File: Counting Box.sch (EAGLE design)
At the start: 3 parts

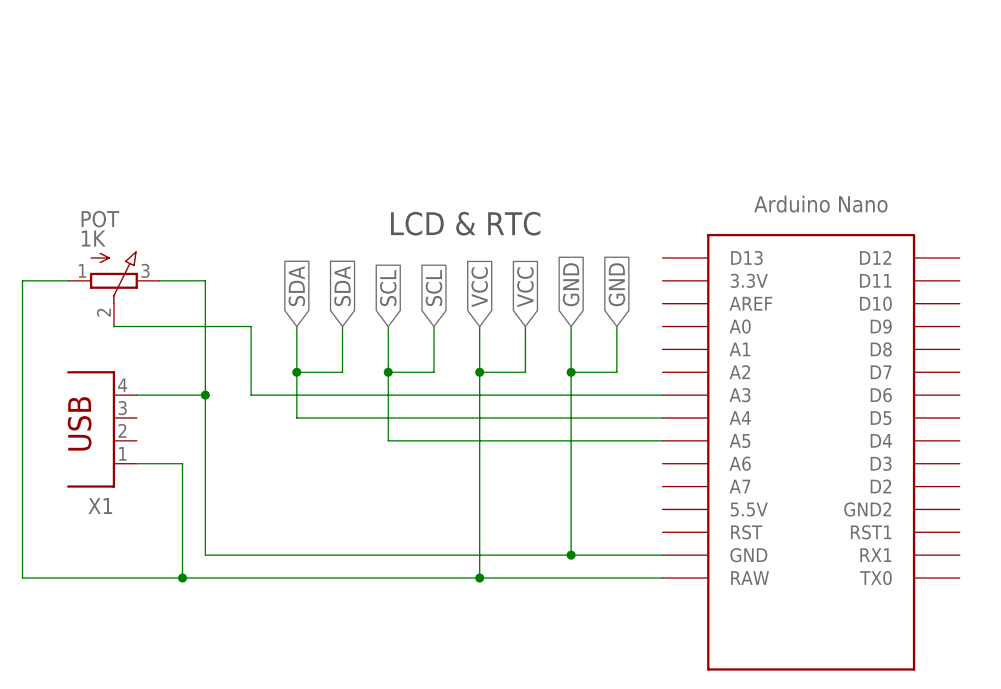
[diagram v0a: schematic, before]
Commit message: Eagle board, code fixes.
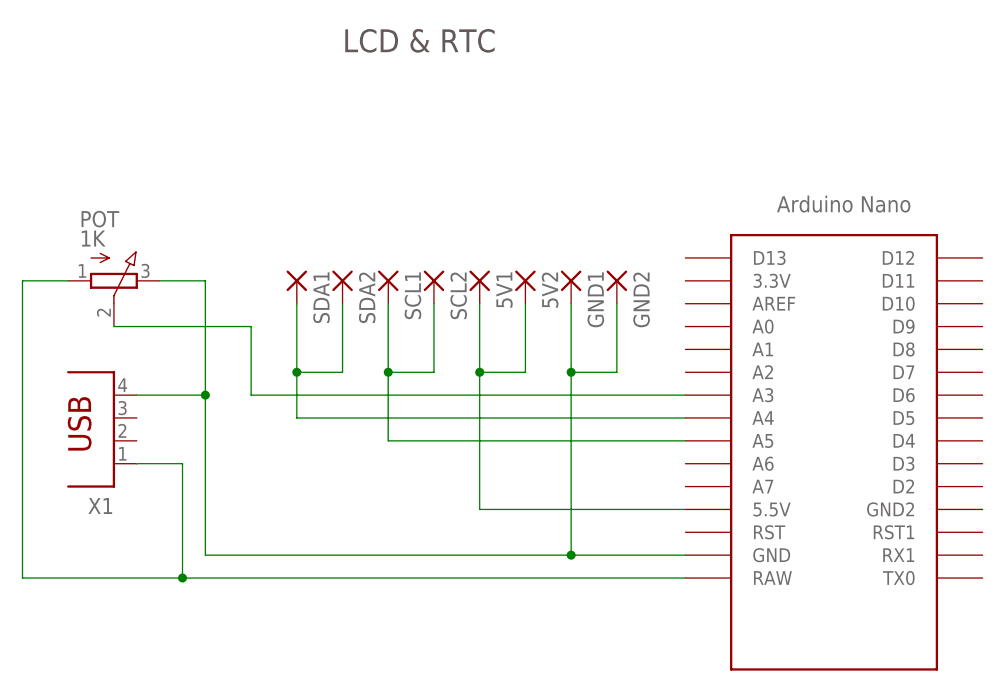
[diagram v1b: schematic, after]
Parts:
- added 5V1, 5V2, GND1, GND2, SCL1, SCL2, SDA1, SDA2: (no value), wirepad:SMD2
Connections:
- net N$3 renamed POT_CTRL
- new net 5V: 5V1.P, 5V2.P, U$1.5.5V
- net GND: now also GND1.P, GND2.P
- net SCL: now also SCL1.P, SCL2.P
- net SDA: now also SDA1.P, SDA2.P
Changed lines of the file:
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@@
 <part name="POT" library="pot" library_urn="urn:adsk.eagle:library:331" deviceset="3RP/1610N" device="" package3d_urn="urn:adsk.eagle:package:22726/1" value="1K"/>
 <part name="X1" library="con-berg" library_urn="urn:adsk.eagle:library:130" deviceset="PN87520" device="" package3d_urn="urn:adsk.eagle:package:6146/1"/>
+<part name="SDA1" library="wirepad" library_urn="urn:adsk.eagle:library:412" deviceset="SMD2" device="" package3d_urn="urn:adsk.eagle:package:30839/1"/>
+<part name="SDA2" library="wirepad" library_urn="urn:adsk.eagle:library:412" deviceset="SMD2" device="" package3d_urn="urn:adsk.eagle:package:30839/1"/>
+<part name="SCL1" library="wirepad" library_urn="urn:adsk.eagle:library:412" deviceset="SMD2" device="" package3d_urn="urn:adsk.eagle:package:30839/1"/>
+<part name="SCL2" library="wirepad" library_urn="urn:adsk.eagle:library:412" deviceset="SMD2" device="" package3d_urn="urn:adsk.eagle:package:30839/1"/>
+<part name="5V1" library="wirepad" library_urn="urn:adsk.eagle:library:412" deviceset="SMD2" device="" package3d_urn="urn:adsk.eagle:package:30839/1"/>
+<part name="5V2" library="wirepad" library_urn="urn:adsk.eagle:library:412" deviceset="SMD2" device="" package3d_urn="urn:adsk.eagle:package:30839/1"/>
+<part name="GND1" library="wirepad" library_urn="urn:adsk.eagle:library:412" deviceset="SMD2" device="" package3d_urn="urn:adsk.eagle:package:30839/1"/>
+<part name="GND2" library="wirepad" library_urn="urn:adsk.eagle:library:412" deviceset="SMD2" device="" package3d_urn="urn:adsk.eagle:package:30839/1"/>
 </parts>
 <sheets>
 <sheet>
 <plain>
-<text x="22.86" y="66.04" size="2.54" layer="97">LCD &amp; RTC</text>
+<text x="17.78" y="86.36" size="2.54" layer="97">LCD &amp; RTC</text>
 </plain>
 <instances>
-<instance part="U$1" gate="G$1" x="76.2" y="48.26"/>
+<instance part="U$1" gate="G$1" x="78.74" y="48.26"/>
 <instance part="POT" gate="G$1" x="-7.62" y="60.96" rot="R270"/>
 <instance part="X1" gate="G$1" x="-7.62" y="45.72" rot="R180"/>
+<instance part="SDA1" gate="1" x="12.7" y="60.96" rot="R270"/>
+<instance part="SDA2" gate="1" x="17.78" y="60.96" rot="R270"/>
+<instance part="SCL1" gate="1" x="22.86" y="60.96" rot="R270"/>
+<instance part="SCL2" gate="1" x="27.94" y="60.96" rot="R270"/>
+<instance part="5V1" gate="1" x="33.02" y="60.96" rot="R270"/>
+<instance part="5V2" gate="1" x="38.1" y="60.96" rot="R270"/>
+<instance part="GND1" gate="1" x="43.18" y="60.96" rot="R270"/>
+<instance part="GND2" gate="1" x="48.26" y="60.96" rot="R270"/>
 </instances>
 <busses>
@@
 <wire x1="0" y1="40.64" x2="0" y2="27.94" width="0.1524" layer="91"/>
 <pinref part="U$1" gate="G$1" pin="RAW"/>
-<wire x1="0" y1="27.94" x2="33.02" y2="27.94" width="0.1524" layer="91"/>
-<wire x1="33.02" y1="27.94" x2="53.34" y2="27.94" width="0.1524" layer="91"/>
+<wire x1="0" y1="27.94" x2="55.88" y2="27.94" width="0.1524" layer="91"/>
 <wire x1="0" y1="27.94" x2="-17.78" y2="27.94" width="0.1524" layer="91"/>
 <junction x="0" y="27.94"/>
@@
 <wire x1="-17.78" y1="27.94" x2="-17.78" y2="60.96" width="0.1524" layer="91"/>
 <wire x1="-17.78" y1="60.96" x2="-12.7" y2="60.96" width="0.1524" layer="91"/>
-<wire x1="33.02" y1="50.8" x2="33.02" y2="27.94" width="0.1524" layer="91"/>
-<junction x="33.02" y="27.94"/>
-<wire x1="33.02" y1="50.8" x2="38.1" y2="50.8" width="0.1524" layer="91"/>
-<wire x1="38.1" y1="50.8" x2="38.1" y2="55.88" width="0.1524" layer="91"/>
-<wire x1="33.02" y1="50.8" x2="33.02" y2="55.88" width="0.1524" layer="91"/>
-<junction x="33.02" y="50.8"/>
-<label x="33.02" y="55.88" size="1.778" layer="95" rot="R90" xref="yes"/>
-<label x="38.1" y="55.88" size="1.778" layer="95" rot="R90" xref="yes"/>
 </segment>
 </net>
@@
 <pinref part="U$1" gate="G$1" pin="GND"/>
 <wire x1="2.54" y1="30.48" x2="43.18" y2="30.48" width="0.1524" layer="91"/>
-<wire x1="43.18" y1="30.48" x2="53.34" y2="30.48" width="0.1524" layer="91"/>
+<wire x1="43.18" y1="30.48" x2="55.88" y2="30.48" width="0.1524" layer="91"/>
 <wire x1="2.54" y1="30.48" x2="2.54" y2="48.26" width="0.1524" layer="91"/>
 <pinref part="POT" gate="G$1" pin="E"/>
@@
 <wire x1="-5.08" y1="48.26" x2="2.54" y2="48.26" width="0.1524" layer="91"/>
 <junction x="2.54" y="48.26"/>
-<wire x1="43.18" y1="55.88" x2="43.18" y2="50.8" width="0.1524" layer="91"/>
+<wire x1="43.18" y1="58.42" x2="43.18" y2="50.8" width="0.1524" layer="91"/>
 <junction x="43.18" y="30.48"/>
 <wire x1="43.18" y1="50.8" x2="43.18" y2="30.48" width="0.1524" layer="91"/>
 <wire x1="43.18" y1="50.8" x2="48.26" y2="50.8" width="0.1524" layer="91"/>
 <junction x="43.18" y="50.8"/>
-<wire x1="48.26" y1="50.8" x2="48.26" y2="55.88" width="0.1524" layer="91"/>
-<label x="43.18" y="55.88" size="1.778" layer="95" rot="R90" xref="yes"/>
-<label x="48.26" y="55.88" size="1.778" layer="95" rot="R90" xref="yes"/>
+<wire x1="48.26" y1="50.8" x2="48.26" y2="58.42" width="0.1524" layer="91"/>
+<pinref part="GND1" gate="1" pin="P"/>
+<pinref part="GND2" gate="1" pin="P"/>
 </segment>
 </net>
-<net name="N$3" class="0">
+<net name="POT_CTRL" class="0">
 <segment>
 <pinref part="U$1" gate="G$1" pin="A3"/>
-<wire x1="53.34" y1="48.26" x2="7.62" y2="48.26" width="0.1524" layer="91"/>
+<wire x1="55.88" y1="48.26" x2="7.62" y2="48.26" width="0.1524" layer="91"/>
 <wire x1="7.62" y1="48.26" x2="7.62" y2="55.88" width="0.1524" layer="91"/>
 <wire x1="7.62" y1="55.88" x2="-7.62" y2="55.88" width="0.1524" layer="91"/>
@@
 <segment>
 <pinref part="U$1" gate="G$1" pin="A4"/>
-<wire x1="53.34" y1="45.72" x2="12.7" y2="45.72" width="0.1524" layer="91"/>
+<wire x1="55.88" y1="45.72" x2="12.7" y2="45.72" width="0.1524" layer="91"/>
 <wire x1="12.7" y1="45.72" x2="12.7" y2="50.8" width="0.1524" layer="91"/>
 <wire x1="12.7" y1="50.8" x2="17.78" y2="50.8" width="0.1524" layer="91"/>
-<wire x1="17.78" y1="50.8" x2="17.78" y2="55.88" width="0.1524" layer="91"/>
-<wire x1="12.7" y1="50.8" x2="12.7" y2="55.88" width="0.1524" layer="91"/>
+<wire x1="17.78" y1="50.8" x2="17.78" y2="58.42" width="0.1524" layer="91"/>
+<wire x1="12.7" y1="50.8" x2="12.7" y2="58.42" width="0.1524" layer="91"/>
 <junction x="12.7" y="50.8"/>
-<label x="12.7" y="55.88" size="1.778" layer="95" rot="R90" xref="yes"/>
-<label x="17.78" y="55.88" size="1.778" layer="95" rot="R90" xref="yes"/>
+<pinref part="SDA1" gate="1" pin="P"/>
+<pinref part="SDA2" gate="1" pin="P"/>
 </segment>
 </net>
@@
 <segment>
 <pinref part="U$1" gate="G$1" pin="A5"/>
-<wire x1="53.34" y1="43.18" x2="22.86" y2="43.18" width="0.1524" layer="91"/>
+<wire x1="55.88" y1="43.18" x2="22.86" y2="43.18" width="0.1524" layer="91"/>
 <wire x1="22.86" y1="43.18" x2="22.86" y2="50.8" width="0.1524" layer="91"/>
 <wire x1="22.86" y1="50.8" x2="27.94" y2="50.8" width="0.1524" layer="91"/>
-<wire x1="27.94" y1="50.8" x2="27.94" y2="55.88" width="0.1524" layer="91"/>
-<wire x1="22.86" y1="50.8" x2="22.86" y2="55.88" width="0.1524" layer="91"/>
+<wire x1="27.94" y1="50.8" x2="27.94" y2="58.42" width="0.1524" layer="91"/>
+<wire x1="22.86" y1="50.8" x2="22.86" y2="58.42" width="0.1524" layer="91"/>
 <junction x="22.86" y="50.8"/>
-<label x="22.86" y="55.88" size="1.778" layer="95" rot="R90" xref="yes"/>
-<label x="27.94" y="55.88" size="1.778" layer="95" rot="R90" xref="yes"/>
+<pinref part="SCL1" gate="1" pin="P"/>
+<pinref part="SCL2" gate="1" pin="P"/>
 </segment>
 </net>
+<net name="5V" class="0">
+<segment>
+<wire x1="38.1" y1="50.8" x2="38.1" y2="58.42" width="0.1524" layer="91"/>
+<wire x1="33.02" y1="50.8" x2="38.1" y2="50.8" width="0.1524" layer="91"/>
+<wire x1="33.02" y1="50.8" x2="33.02" y2="58.42" width="0.1524" layer="91"/>
+<junction x="33.02" y="50.8"/>
+<wire x1="33.02" y1="50.8" x2="33.02" y2="35.56" width="0.1524" layer="91"/>
+<pinref part="U$1" gate="G$1" pin="5.5V"/>
+<wire x1="55.88" y1="35.56" x2="33.02" y2="35.56" width="0.1524" layer="91"/>
+<pinref part="5V1" gate="1" pin="P"/>
+<pinref part="5V2" gate="1" pin="P"/>
+</segment>
+</net>

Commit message: Added second potentiometer to schematic.
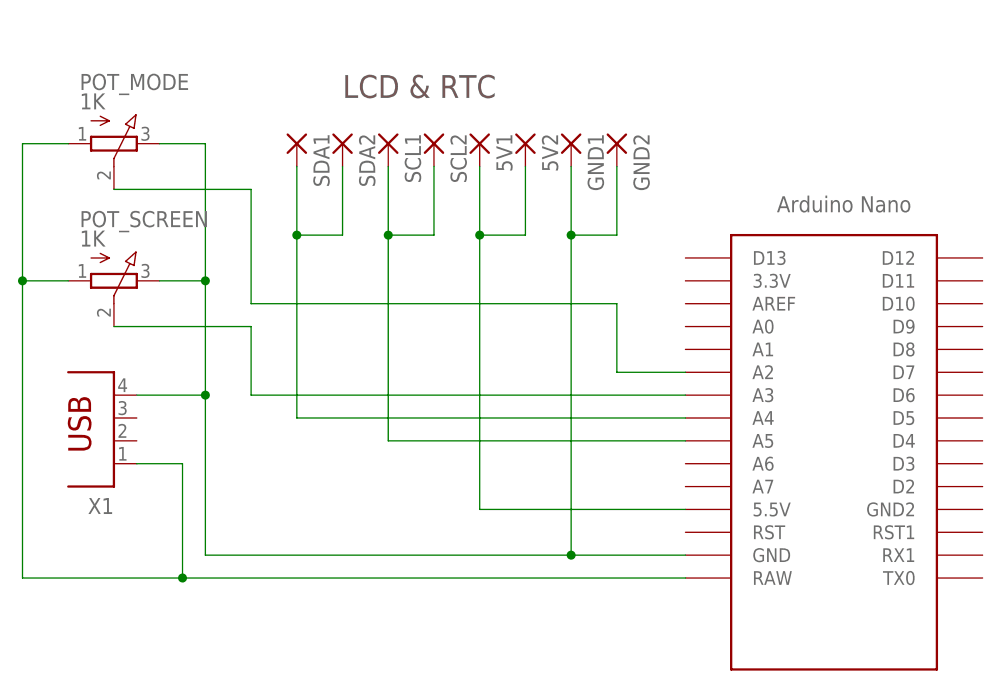
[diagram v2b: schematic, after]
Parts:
- added POT_MODE: 1K, pot:3RP/1610N
- renumbered POT to POT_SCREEN
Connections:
- new net N$5: POT_MODE.S, U$1.A2
- net GND: now also POT_MODE.E
- net VCC: now also POT_MODE.A
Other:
- moved on the sheet: 5V1, 5V2, GND1, GND2, SCL1, SCL2, SDA1, SDA2
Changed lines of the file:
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@@
 <?xml version="1.0" encoding="utf-8"?>
 <!DOCTYPE eagle SYSTEM "eagle.dtd">
-<eagle version="8.4.0">
+<eagle version="8.5.1">
 <drawing>
 <settings>
@@
 <parts>
 <part name="U$1" library="Arduino-clone" deviceset="NANO" device=""/>
-<part name="POT" library="pot" library_urn="urn:adsk.eagle:library:331" deviceset="3RP/1610N" device="" package3d_urn="urn:adsk.eagle:package:22726/1" value="1K"/>
+<part name="POT_SCREEN" library="pot" library_urn="urn:adsk.eagle:library:331" deviceset="3RP/1610N" device="" package3d_urn="urn:adsk.eagle:package:22726/1" value="1K"/>
 <part name="X1" library="con-berg" library_urn="urn:adsk.eagle:library:130" deviceset="PN87520" device="" package3d_urn="urn:adsk.eagle:package:6146/1"/>
 <part name="SDA1" library="wirepad" library_urn="urn:adsk.eagle:library:412" deviceset="SMD2" device="" package3d_urn="urn:adsk.eagle:package:30839/1"/>
@@
 <part name="GND1" library="wirepad" library_urn="urn:adsk.eagle:library:412" deviceset="SMD2" device="" package3d_urn="urn:adsk.eagle:package:30839/1"/>
 <part name="GND2" library="wirepad" library_urn="urn:adsk.eagle:library:412" deviceset="SMD2" device="" package3d_urn="urn:adsk.eagle:package:30839/1"/>
+<part name="POT_MODE" library="pot" library_urn="urn:adsk.eagle:library:331" deviceset="3RP/1610N" device="" package3d_urn="urn:adsk.eagle:package:22726/1" value="1K"/>
 </parts>
 <sheets>
 <sheet>
 <plain>
-<text x="17.78" y="86.36" size="2.54" layer="97">LCD &amp; RTC</text>
+<text x="17.78" y="81.28" size="2.54" layer="97">LCD &amp; RTC</text>
 </plain>
 <instances>
 <instance part="U$1" gate="G$1" x="78.74" y="48.26"/>
-<instance part="POT" gate="G$1" x="-7.62" y="60.96" rot="R270"/>
+<instance part="POT_SCREEN" gate="G$1" x="-7.62" y="60.96" rot="R270"/>
 <instance part="X1" gate="G$1" x="-7.62" y="45.72" rot="R180"/>
-<instance part="SDA1" gate="1" x="12.7" y="60.96" rot="R270"/>
-<instance part="SDA2" gate="1" x="17.78" y="60.96" rot="R270"/>
-<instance part="SCL1" gate="1" x="22.86" y="60.96" rot="R270"/>
-<instance part="SCL2" gate="1" x="27.94" y="60.96" rot="R270"/>
-<instance part="5V1" gate="1" x="33.02" y="60.96" rot="R270"/>
-<instance part="5V2" gate="1" x="38.1" y="60.96" rot="R270"/>
-<instance part="GND1" gate="1" x="43.18" y="60.96" rot="R270"/>
-<instance part="GND2" gate="1" x="48.26" y="60.96" rot="R270"/>
+<instance part="SDA1" gate="1" x="12.7" y="76.2" rot="R270"/>
+<instance part="SDA2" gate="1" x="17.78" y="76.2" rot="R270"/>
+<instance part="SCL1" gate="1" x="22.86" y="76.2" rot="R270"/>
+<instance part="SCL2" gate="1" x="27.94" y="76.2" rot="R270"/>
+<instance part="5V1" gate="1" x="33.02" y="76.2" rot="R270"/>
+<instance part="5V2" gate="1" x="38.1" y="76.2" rot="R270"/>
+<instance part="GND1" gate="1" x="43.18" y="76.2" rot="R270"/>
+<instance part="GND2" gate="1" x="48.26" y="76.2" rot="R270"/>
+<instance part="POT_MODE" gate="G$1" x="-7.62" y="76.2" rot="R270"/>
 </instances>
 <busses>
@@
 <wire x1="0" y1="27.94" x2="-17.78" y2="27.94" width="0.1524" layer="91"/>
 <junction x="0" y="27.94"/>
-<pinref part="POT" gate="G$1" pin="A"/>
+<pinref part="POT_SCREEN" gate="G$1" pin="A"/>
 <wire x1="-17.78" y1="27.94" x2="-17.78" y2="60.96" width="0.1524" layer="91"/>
 <wire x1="-17.78" y1="60.96" x2="-12.7" y2="60.96" width="0.1524" layer="91"/>
+<wire x1="-17.78" y1="60.96" x2="-17.78" y2="76.2" width="0.1524" layer="91"/>
+<junction x="-17.78" y="60.96"/>
+<pinref part="POT_MODE" gate="G$1" pin="A"/>
+<wire x1="-17.78" y1="76.2" x2="-12.7" y2="76.2" width="0.1524" layer="91"/>
 </segment>
 </net>
@@
 <wire x1="43.18" y1="30.48" x2="55.88" y2="30.48" width="0.1524" layer="91"/>
 <wire x1="2.54" y1="30.48" x2="2.54" y2="48.26" width="0.1524" layer="91"/>
-<pinref part="POT" gate="G$1" pin="E"/>
+<pinref part="POT_SCREEN" gate="G$1" pin="E"/>
 <wire x1="2.54" y1="48.26" x2="2.54" y2="60.96" width="0.1524" layer="91"/>
 <wire x1="2.54" y1="60.96" x2="-2.54" y2="60.96" width="0.1524" layer="91"/>
@@
 <wire x1="-5.08" y1="48.26" x2="2.54" y2="48.26" width="0.1524" layer="91"/>
 <junction x="2.54" y="48.26"/>
-<wire x1="43.18" y1="58.42" x2="43.18" y2="50.8" width="0.1524" layer="91"/>
+<wire x1="43.18" y1="73.66" x2="43.18" y2="66.04" width="0.1524" layer="91"/>
 <junction x="43.18" y="30.48"/>
-<wire x1="43.18" y1="50.8" x2="43.18" y2="30.48" width="0.1524" layer="91"/>
-<wire x1="43.18" y1="50.8" x2="48.26" y2="50.8" width="0.1524" layer="91"/>
-<junction x="43.18" y="50.8"/>
-<wire x1="48.26" y1="50.8" x2="48.26" y2="58.42" width="0.1524" layer="91"/>
+<wire x1="43.18" y1="66.04" x2="43.18" y2="30.48" width="0.1524" layer="91"/>
+<wire x1="43.18" y1="66.04" x2="48.26" y2="66.04" width="0.1524" layer="91"/>
+<junction x="43.18" y="66.04"/>
+<wire x1="48.26" y1="66.04" x2="48.26" y2="73.66" width="0.1524" layer="91"/>
 <pinref part="GND1" gate="1" pin="P"/>
 <pinref part="GND2" gate="1" pin="P"/>
+<pinref part="POT_MODE" gate="G$1" pin="E"/>
+<wire x1="-2.54" y1="76.2" x2="2.54" y2="76.2" width="0.1524" layer="91"/>
+<wire x1="2.54" y1="76.2" x2="2.54" y2="60.96" width="0.1524" layer="91"/>
+<junction x="2.54" y="60.96"/>
 </segment>
 </net>
@@
 <wire x1="7.62" y1="48.26" x2="7.62" y2="55.88" width="0.1524" layer="91"/>
 <wire x1="7.62" y1="55.88" x2="-7.62" y2="55.88" width="0.1524" layer="91"/>
-<pinref part="POT" gate="G$1" pin="S"/>
+<pinref part="POT_SCREEN" gate="G$1" pin="S"/>
 </segment>
 </net>
@@
 <pinref part="U$1" gate="G$1" pin="A4"/>
 <wire x1="55.88" y1="45.72" x2="12.7" y2="45.72" width="0.1524" layer="91"/>
-<wire x1="12.7" y1="45.72" x2="12.7" y2="50.8" width="0.1524" layer="91"/>
-<wire x1="12.7" y1="50.8" x2="17.78" y2="50.8" width="0.1524" layer="91"/>
-<wire x1="17.78" y1="50.8" x2="17.78" y2="58.42" width="0.1524" layer="91"/>
-<wire x1="12.7" y1="50.8" x2="12.7" y2="58.42" width="0.1524" layer="91"/>
-<junction x="12.7" y="50.8"/>
+<wire x1="12.7" y1="45.72" x2="12.7" y2="66.04" width="0.1524" layer="91"/>
+<wire x1="12.7" y1="66.04" x2="17.78" y2="66.04" width="0.1524" layer="91"/>
+<wire x1="17.78" y1="66.04" x2="17.78" y2="73.66" width="0.1524" layer="91"/>
+<wire x1="12.7" y1="66.04" x2="12.7" y2="73.66" width="0.1524" layer="91"/>
+<junction x="12.7" y="66.04"/>
 <pinref part="SDA1" gate="1" pin="P"/>
 <pinref part="SDA2" gate="1" pin="P"/>
@@
 <pinref part="U$1" gate="G$1" pin="A5"/>
 <wire x1="55.88" y1="43.18" x2="22.86" y2="43.18" width="0.1524" layer="91"/>
-<wire x1="22.86" y1="43.18" x2="22.86" y2="50.8" width="0.1524" layer="91"/>
-<wire x1="22.86" y1="50.8" x2="27.94" y2="50.8" width="0.1524" layer="91"/>
-<wire x1="27.94" y1="50.8" x2="27.94" y2="58.42" width="0.1524" layer="91"/>
-<wire x1="22.86" y1="50.8" x2="22.86" y2="58.42" width="0.1524" layer="91"/>
-<junction x="22.86" y="50.8"/>
+<wire x1="22.86" y1="43.18" x2="22.86" y2="66.04" width="0.1524" layer="91"/>
+<wire x1="22.86" y1="66.04" x2="27.94" y2="66.04" width="0.1524" layer="91"/>
+<wire x1="27.94" y1="66.04" x2="27.94" y2="73.66" width="0.1524" layer="91"/>
+<wire x1="22.86" y1="66.04" x2="22.86" y2="73.66" width="0.1524" layer="91"/>
+<junction x="22.86" y="66.04"/>
 <pinref part="SCL1" gate="1" pin="P"/>
 <pinref part="SCL2" gate="1" pin="P"/>
@@
 <net name="5V" class="0">
 <segment>
-<wire x1="38.1" y1="50.8" x2="38.1" y2="58.42" width="0.1524" layer="91"/>
-<wire x1="33.02" y1="50.8" x2="38.1" y2="50.8" width="0.1524" layer="91"/>
-<wire x1="33.02" y1="50.8" x2="33.02" y2="58.42" width="0.1524" layer="91"/>
-<junction x="33.02" y="50.8"/>
-<wire x1="33.02" y1="50.8" x2="33.02" y2="35.56" width="0.1524" layer="91"/>
+<wire x1="38.1" y1="66.04" x2="38.1" y2="73.66" width="0.1524" layer="91"/>
+<wire x1="33.02" y1="66.04" x2="38.1" y2="66.04" width="0.1524" layer="91"/>
+<wire x1="33.02" y1="66.04" x2="33.02" y2="73.66" width="0.1524" layer="91"/>
+<junction x="33.02" y="66.04"/>
+<wire x1="33.02" y1="66.04" x2="33.02" y2="35.56" width="0.1524" layer="91"/>
 <pinref part="U$1" gate="G$1" pin="5.5V"/>
 <wire x1="55.88" y1="35.56" x2="33.02" y2="35.56" width="0.1524" layer="91"/>
@@
 </segment>
 </net>
+<net name="N$5" class="0">
+<segment>
+<pinref part="POT_MODE" gate="G$1" pin="S"/>
+<wire x1="-7.62" y1="71.12" x2="7.62" y2="71.12" width="0.1524" layer="91"/>
+<wire x1="7.62" y1="71.12" x2="7.62" y2="58.42" width="0.1524" layer="91"/>
+<wire x1="7.62" y1="58.42" x2="48.26" y2="58.42" width="0.1524" layer="91"/>
+<wire x1="48.26" y1="58.42" x2="48.26" y2="50.8" width="0.1524" layer="91"/>
+<pinref part="U$1" gate="G$1" pin="A2"/>
+<wire x1="48.26" y1="50.8" x2="55.88" y2="50.8" width="0.1524" layer="91"/>
+</segment>
+</net>

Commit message: DateTime to timestamp conversion.
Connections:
- net N$5 renamed POT_MODE
- net POT_CTRL renamed POT_SCREEN
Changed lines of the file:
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@@
 </segment>
 </net>
-<net name="POT_CTRL" class="0">
+<net name="POT_SCREEN" class="0">
 <segment>
 <pinref part="U$1" gate="G$1" pin="A3"/>
@@
 </segment>
 </net>
-<net name="N$5" class="0">
+<net name="POT_MODE" class="0">
 <segment>
 <pinref part="POT_MODE" gate="G$1" pin="S"/>
